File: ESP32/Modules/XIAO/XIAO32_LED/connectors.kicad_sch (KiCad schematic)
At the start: 5 parts, among them J1 Conn_01x03_Pin, J2 Conn_01x03_Pin, J3 Conn_01x02_Pin, J4 Conn_01x02_Pin, SW1 SW_SPDT

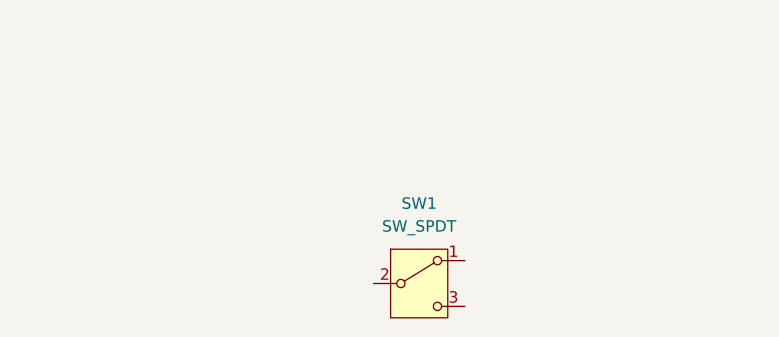
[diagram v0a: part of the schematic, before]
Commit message: Initial wiring of Power and Connectors pages
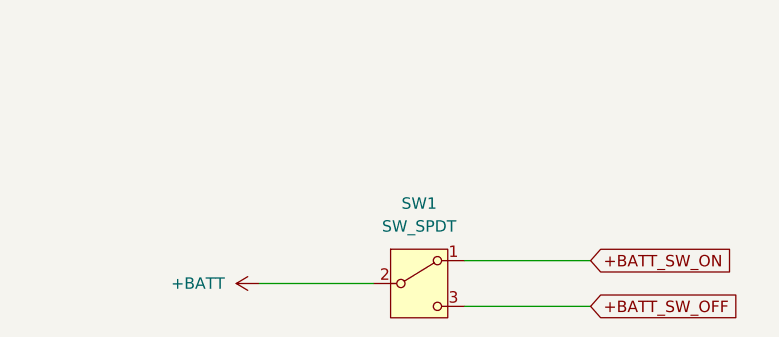
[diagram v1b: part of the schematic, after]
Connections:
- net +BATT_SW_ON: now reaches SW1.1 (A)
- net +BATT: now reaches SW1.2 (B)
- net +BATT_SW_OFF: now reaches SW1.3 (C)
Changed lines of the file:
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@@
 	(generator_version "9.0")
 	(paper "A4")
+	(wire
+		(pts
+			(xy 193.04 121.92) (xy 207.01 121.92)
+		)
+		(stroke
+			(width 0)
+			(type default)
+		)
+	)
+	(wire
+		(pts
+			(xy 193.04 116.84) (xy 207.01 116.84)
+		)
+		(stroke
+			(width 0)
+			(type default)
+		)
+	)
+	(wire
+		(pts
+			(xy 170.18 119.38) (xy 182.88 119.38)
+		)
+		(stroke
+			(width 0)
+			(type default)
+		)
+	)
+	(global_label "+BATT_SW_ON"
+		(shape input)
+		(at 207.01 116.84 0)
+		(fields_autoplaced yes)
+		(effects
+			(font
+				(size 1.27 1.27)
+			)
+			(justify left)
+		)
+		(property "Intersheetrefs" "${INTERSHEET_REFS}"
+			(at 223.1185 116.84 0)
+			(effects
+				(font
+					(size 1.27 1.27)
+				)
+				(justify left)
+				(hide yes)
+			)
+		)
+	)
+	(global_label "+BATT_SW_OFF"
+		(shape input)
+		(at 207.01 121.92 0)
+		(fields_autoplaced yes)
+		(effects
+			(font
+				(size 1.27 1.27)
+			)
+			(justify left)
+		)
+		(property "Intersheetrefs" "${INTERSHEET_REFS}"
+			(at 223.9652 121.92 0)
+			(effects
+				(font
+					(size 1.27 1.27)
+				)
+				(justify left)
+				(hide yes)
+			)
+		)
+	)
 	(symbol
 		(lib_id "Connector:Conn_01x02_Pin")
@@
 					(unit 1)
 				)
+			)
+		)
+	)
+	(symbol
+		(lib_id "power:+BATT")
+		(at 170.18 119.38 90)
+		(unit 1)
+		(exclude_from_sim no)
+		(in_bom yes)
+		(on_board yes)
+		(dnp no)
+		(fields_autoplaced yes)
+		(property "Reference" "#PWR04"
+			(at 173.99 119.38 0)
+			(effects
+				(font
+					(size 1.27 1.27)
+				)
+				(hide yes)
+			)
+		)
+		(property "Value" "+BATT"
+			(at 166.37 119.3799 90)
+			(effects
+				(font
+					(size 1.27 1.27)
+				)
+				(justify left)
+			)
+		)
+		(property "Footprint" ""
+			(at 170.18 119.38 0)
+			(effects
+				(font
+					(size 1.27 1.27)
+				)
+				(hide yes)
+			)
+		)
+		(property "Datasheet" ""
+			(at 170.18 119.38 0)
+			(effects
+				(font
+					(size 1.27 1.27)
+				)
+				(hide yes)
+			)
+		)
+		(property "Description" "Power symbol creates a global label with name \"+BATT\""
+			(at 170.18 119.38 0)
+			(effects
+				(font
+					(size 1.27 1.27)
+				)
+				(hide yes)
+			)
+		)
+		(pin "1"
+		)
+		(instances
+			(project ""
+				(path "/68368358-b5ad-4b4d-9ad1-c8762dcf4755/00c2a9f3-48c2-46aa-88b4-de5fc390d021"
+					(reference "#PWR04")
+					(unit 1)
+				)

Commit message: XIAO32_LED: MCU wired up
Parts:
- removed SW1: SW_SPDT, symbol Switch:SW_SPDT
- J1: value Conn_01x03_Pin -> LED0
- J2: value Conn_01x03_Pin -> LED1
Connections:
- net +5V: now reaches J2.1 (Pin_1)
- net +5V: now also J1.1 (Pin_1)
- net LED1_DATA_5V: now reaches J2.2 (Pin_2)
- net LED0_DATA_5V: now reaches J1.2 (Pin_2)
- net GND: now reaches J1.3 (Pin_3)
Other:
- moved on the sheet: J2
